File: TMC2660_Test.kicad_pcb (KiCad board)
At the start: 2 copper layers, 62 parts, among them P101 CONN_4, P102 CONN_4, P103 CONN_2, P104 CONN_13X2, P105 CONN_4, P106 CONN_4, P107 CONN_1, P108 CONN_1, P109 CONN_1, P110 CONN_1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

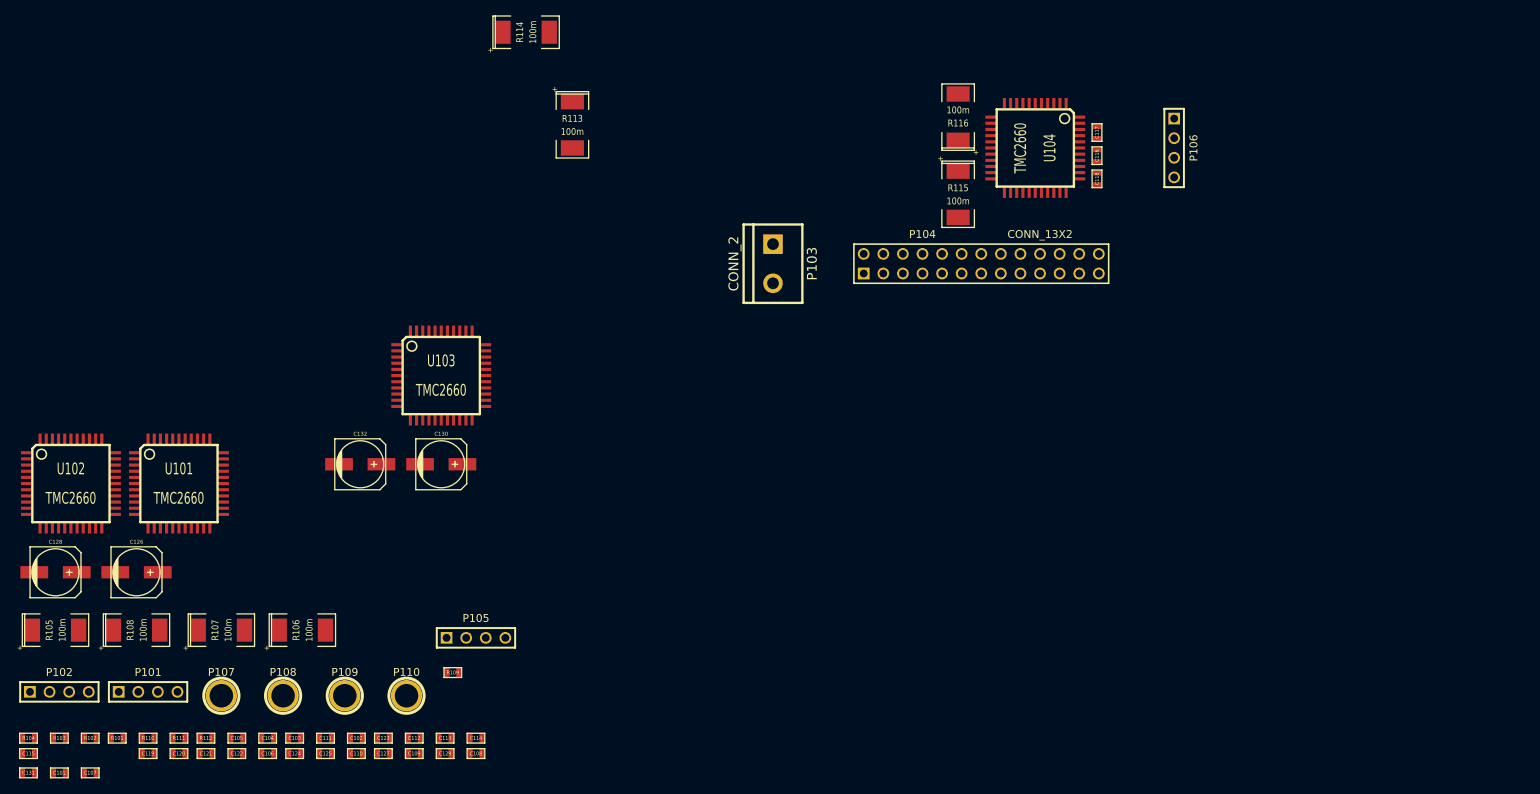
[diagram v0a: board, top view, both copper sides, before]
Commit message: Change alu. caps to thru hole.
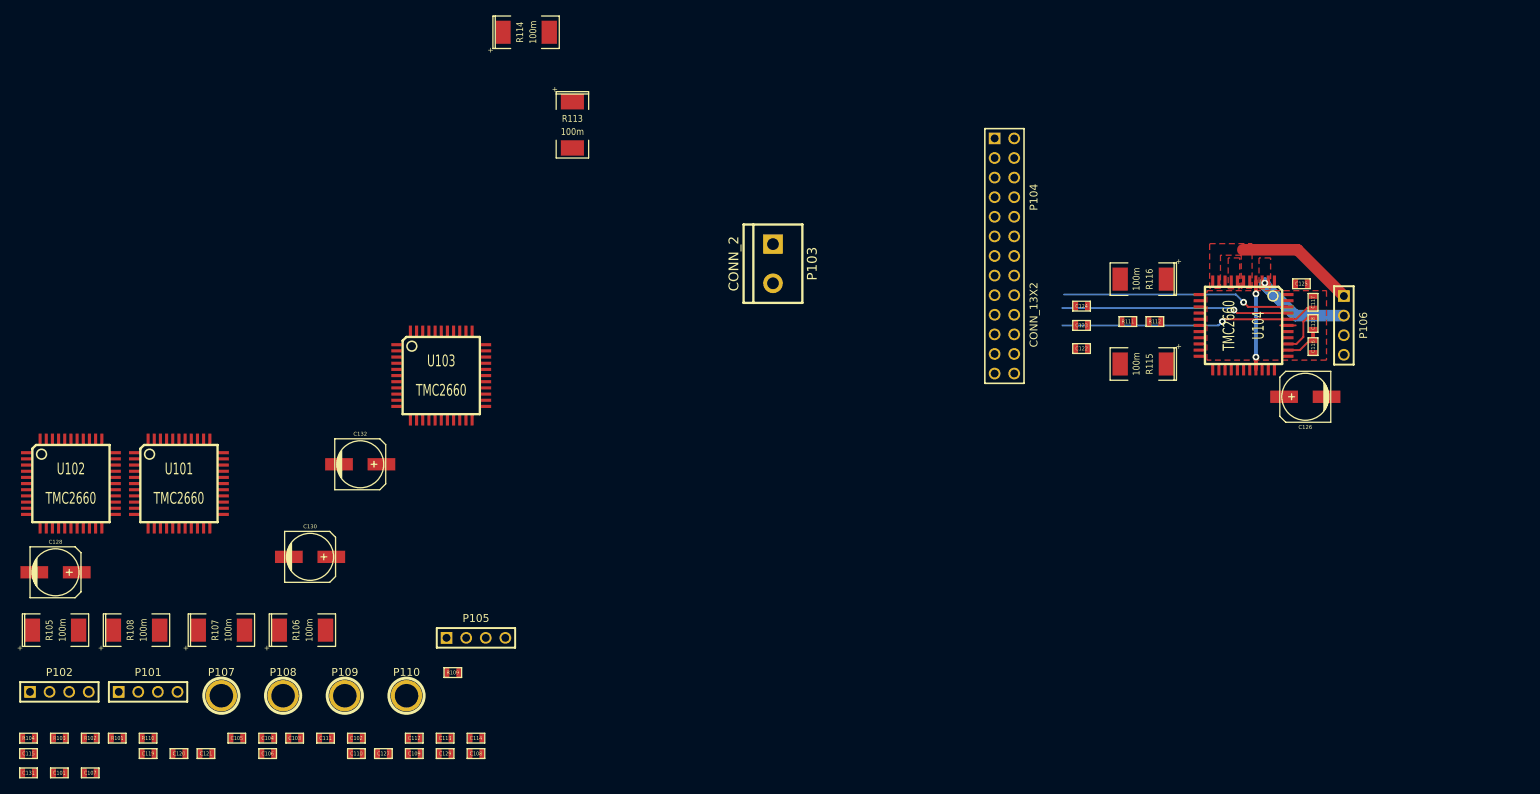
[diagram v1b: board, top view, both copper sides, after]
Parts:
- moved C126 153.2 mm to (185.0, 134.2), turned to 180 degrees
- moved C125 140.4 mm to (184.5, 119.6)
- moved R111 134.3 mm to (162.0, 124.5)
- moved R112 134.3 mm to (165.5, 124.5)
- moved C122 121.4 mm to (156.0, 128.0)
- moved C124 117.3 mm to (156.0, 122.5)
- moved C123 105.1 mm to (156.0, 125.0)
- moved C116 37.4 mm to (186.0, 127.8), turned to 90 degrees
- moved C117 35.6 mm to (186.0, 122.0)
- moved U104 35.5 mm to (177.0, 125.0)
- moved C118 33.7 mm to (186.0, 124.8), turned to 90 degrees
- moved R115 32.6 mm to (164.0, 130.0), turned to 180 degrees
- moved R116 31.9 mm to (164.0, 119.0), turned to 180 degrees
- moved P106 31.8 mm to (190.0, 125.0)
- moved C130 20.8 mm to (56.0, 155.0)
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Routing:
- net VCC: track 0.00 -> 33.4 mm, vias 0 -> 1
- net E-STEP: track 0.00 -> 29.6 mm, vias 0 -> 1
- net E-DIR: track 0.00 -> 29.5 mm, vias 0 -> 1
- net +12V: track 0.00 -> 16.7 mm, vias 0 -> 2
- net N-0000051: track 0.00 -> 15.6 mm
- net N-0000013: track 0.00 -> 12.1 mm, vias 0 -> 1
- net N-0000015: track 0.00 -> 5.87 mm
- net GND: track 0.00 -> 2.00 mm
- added copper zone on F.Cu, net GND
- added copper zone on F.Cu, net N-0000013
- added copper zone on F.Cu, net N-0000051
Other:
- net class Default: clearance 0.254 -> 0.152
- rule trace_clearance: 0.254 -> 0.152
- rule trace_min: 0.254 -> 0.154

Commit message: One chip sorta laid out.
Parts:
- C126, C128, C130, C132: footprint c_elec_6.3x7.7 -> C1V5
- moved C128 144.2 mm to (162.6, 120.9), turned to 270 degrees
- moved C127 128.9 mm to (184.3, 130.4)
- moved C126 23.1 mm to (162.6, 128.5), turned to 90 degrees
- moved C123 16.8 mm to (171.2, 117.9), turned to 180 degrees
- moved C122 15.8 mm to (171.3, 131.9), turned to 180 degrees
- moved R111 13.9 mm to (171.8, 134.4), turned to 90 degrees
- moved C124 12.4 mm to (168.4, 121.5), turned to 180 degrees
- moved R112 10.8 mm to (171.7, 115.7), turned to 90 degrees
- moved R115 4.59 mm to (164.9, 134.5)
- moved R116 3.49 mm to (164.8, 115.6)
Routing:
- net +12V: track 16.7 -> 52.4 mm
- net GND: track 2.00 -> 34.9 mm, vias 0 -> 17
- net N-0000051: track 15.6 -> 0.00 mm
- net N-0000013: track 12.1 -> 0.00 mm, vias 1 -> 0
- net N-0000048: track 0.00 -> 11.5 mm
- net N-0000045: track 0.00 -> 11.4 mm
- net N-0000046: track 0.00 -> 7.74 mm
- net N-0000047: track 0.00 -> 7.65 mm
- net E-STEP: track 29.6 -> 24.0 mm
- net E-DIR: track 29.5 -> 24.6 mm
- net VCC: track 33.4 -> 28.6 mm
- net N-0000012: track 0.00 -> 2.25 mm
- added copper zone on B.Cu, net GND
- added copper zone on B.Cu, net N-0000013
- added copper zone on B.Cu, net N-0000049
- added copper zone on F.Cu, net N-0000049
- added copper zone on F.Cu, net N-0000050

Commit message: Getting the layout close to complete
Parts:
- added C133: 1u, SM0603, F.Cu at (204.0, 99.5)
- added C134: 47u, C1V5, F.Cu at (105.7, 178.1)
- added C135: 1u, SM0603, F.Cu at (94.1, 161.7)
- added C136: 47u, C1V5, F.Cu at (87.0, 180.8)
- added C137: 1u, SM0603, F.Cu at (203.8, 111.7)
- added C138: 47u, C1V5, F.Cu at (109.7, 165.4)
- added C139: 1u, SM0603, F.Cu at (93.7, 163.5)
- added C140: 47u, C1V5, F.Cu at (92.5, 172.6)
- moved P102 198.0 mm to (209.8, 105.4), turned to 270 degrees
- moved R104 190.8 mm to (191.5, 95.9), turned to 90 degrees
- moved R103 179.5 mm to (191.4, 114.9), turned to 90 degrees
- moved U102 176.4 mm to (196.8, 105.4), turned to 270 degrees
- moved C104 172.8 mm to (205.7, 102.5), turned to 270 degrees
- moved C106 172.4 mm to (205.7, 105.4), turned to 90 degrees
- moved R108 166.0 mm to (184.8, 96.1), turned to 180 degrees
- moved C102 159.8 mm to (205.6, 108.5), turned to 90 degrees
- moved C110 152.9 mm to (191.0, 98.5), turned to 180 degrees
- moved R107 148.6 mm to (184.4, 114.3), turned to 180 degrees
- moved C112 140.4 mm to (187.8, 102.9)
- moved C109 139.5 mm to (190.9, 111.7), turned to 180 degrees
- moved C130 135.3 mm to (183.2, 108.9), turned to 90 degrees
- moved C132 127.7 mm to (183.2, 101.2), turned to 270 degrees
- moved P103 61.6 mm to (174.0, 137.8), turned to 0 degrees
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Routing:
- net GND: track 34.9 -> 22.5 mm, vias 17 -> 9
- added copper zone on F.Cu, net N-0000013
- added copper zone on F.Cu, net N-0000028
- added copper zone on B.Cu, net N-0000077
- added copper zone on F.Cu, net N-0000077
- added copper zone on B.Cu, net N-0000082
- added copper zone on F.Cu, net N-0000082
- added copper zone on F.Cu, net N-0000083
- added copper zone on F.Cu, net N-0000089
- removed copper zone on B.Cu, net GND
- removed copper zone on F.Cu, net N-0000018

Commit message: Everything is approximately where it should be. Now to draw all the damn fills and lines.
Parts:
- moved P107 168.8 mm to (209.8, 138.8), turned to 90 degrees
- moved P110 161.3 mm to (209.8, 95.3), turned to 90 degrees
- moved C107 155.7 mm to (157.2, 96.8), turned to 90 degrees
- moved R105 155.0 mm to (164.7, 101.8)
- moved R101 149.5 mm to (157.9, 99.5), turned to 180 degrees
- moved R102 146.8 mm to (158.0, 111.2)
- moved C101 143.9 mm to (142.6, 102.3), turned to 270 degrees
- moved C131 143.4 mm to (143.6, 111.2), turned to 180 degrees
- moved C119 135.6 mm to (156.7, 120.8), turned to 90 degrees
- moved C115 133.1 mm to (142.8, 130.3), turned to 270 degrees
- moved R110 130.0 mm to (158.0, 136.4)
- moved C121 126.4 mm to (159.8, 133.5)
- moved C120 125.5 mm to (157.4, 139.0), turned to 270 degrees
- moved C111 124.3 mm to (160.0, 107.5), turned to 90 degrees
- moved R106 123.7 mm to (165.6, 109.1)
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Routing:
- net VCC: track 28.6 -> 69.0 mm
- net +12V: track 52.4 -> 19.6 mm, vias 2 -> 0
- net GND: track 22.5 -> 9.05 mm, vias 9 -> 0
- net E-STEP: track 24.0 -> 30.3 mm
- net N-0000047: track 11.5 -> 5.96 mm
- net E-DIR: track 24.6 -> 29.7 mm
- net N-0000048: track 11.4 -> 7.52 mm
- net N-0000049: track 7.74 -> 6.37 mm
- net N-0000046: track 7.65 -> 6.71 mm
- net N-0000016: track 2.25 -> 2.84 mm
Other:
- board outline added: 77.7 x 49.9 mm

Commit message: Work on filled zones.
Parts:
- moved R108 2.24 mm to (182.9, 101.3)
- moved C120 1.00 mm to (157.5, 138.0)
- moved C137 1.00 mm to (204.6, 111.1)
- moved R107 0.99 mm to (184.2, 109.2)
- moved R110 0.89 mm to (158.4, 135.6)
- moved C135 0.71 mm to (143.5, 124.2)
- moved P105 0.70 mm to (138.6, 129.8)
- moved U103 0.70 mm to (151.6, 129.8)
- moved C114 0.60 mm to (142.8, 132.7)
- moved C115 0.60 mm to (142.8, 129.7)
- moved C113 0.60 mm to (142.8, 126.8)
- moved C112 0.32 mm to (188.4, 101.3)
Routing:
- net +12V: track 19.6 -> 285.4 mm
- net N-0000087: track 0.00 -> 7.05 mm
- net N-0000085: track 0.00 -> 6.90 mm
- net N-0000086: track 0.00 -> 6.84 mm
- net N-0000084: track 0.00 -> 5.61 mm
- net N-0000088: track 0.00 -> 5.52 mm
- net GND: track 9.05 -> 13.6 mm
- net VCC: track 69.0 -> 72.8 mm
- added copper zone on B.Cu, net N-0000063
- added copper zone on F.Cu, net N-0000063
- added copper zone on B.Cu, net N-0000073

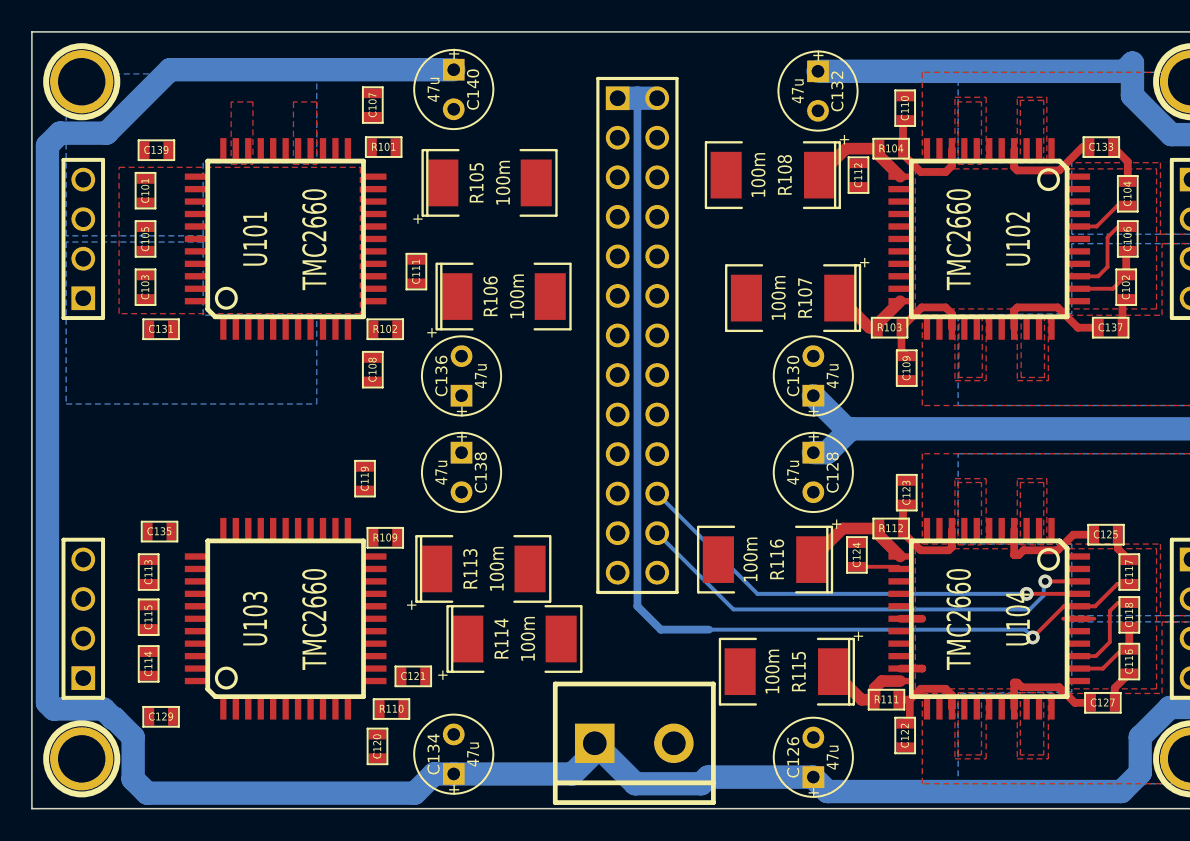
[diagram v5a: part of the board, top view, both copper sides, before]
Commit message: Finished all the power connections and varios R and Cs connected to the chips. Still to do: ground plane, signal lines, connect motor planes properly.
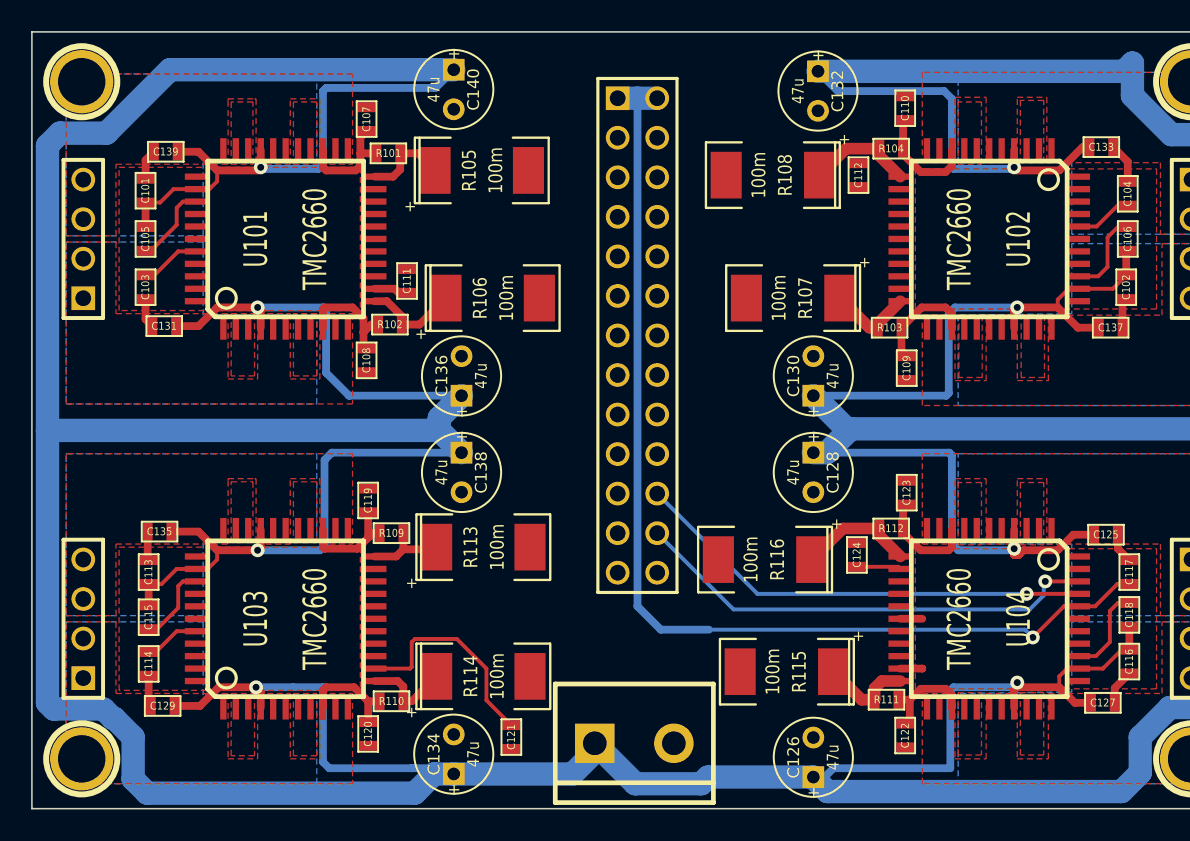
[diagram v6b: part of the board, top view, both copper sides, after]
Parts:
- moved C121 7.41 mm to (166.1, 137.4), turned to 270 degrees
- moved R114 3.12 mm to (164.3, 133.5)
- moved C119 1.41 mm to (156.9, 122.2)
- moved R113 1.40 mm to (164.3, 125.2)
- moved C120 1.00 mm to (156.9, 137.2)
- moved C107 0.98 mm to (156.8, 97.7)
- moved R105 0.94 mm to (164.2, 101.0)
- moved C111 0.85 mm to (159.4, 108.1)
- moved C108 0.72 mm to (156.8, 113.2)
- moved R106 0.71 mm to (164.9, 109.2)
- moved C129 0.71 mm to (143.7, 135.4)
- moved C139 0.61 mm to (143.9, 99.8)
- moved R109 0.50 mm to (158.4, 124.3)
- moved R110 0.50 mm to (158.4, 135.1)
- moved R101 0.50 mm to (158.2, 99.9)
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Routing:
- net +12V: track 285.4 -> 508.9 mm, vias 0 -> 8
- net N-0000020: track 0.00 -> 14.0 mm
- net VCC: track 72.8 -> 80.3 mm
- net N-0000052: track 0.00 -> 7.31 mm
- net N-0000054: track 0.00 -> 7.16 mm
- net N-0000022: track 0.00 -> 6.85 mm
- net N-0000023: track 0.00 -> 6.55 mm
- net N-0000056: track 0.00 -> 6.23 mm
- net GND: track 13.6 -> 19.4 mm
- net N-0000021: track 0.00 -> 5.74 mm
- net N-0000053: track 0.00 -> 5.57 mm
- net N-0000019: track 0.00 -> 5.27 mm
- net N-0000068: track 0.00 -> 5.24 mm
- net N-0000079: track 0.00 -> 5.17 mm
- net N-0000055: track 0.00 -> 2.19 mm
- added copper zone on B.Cu, net N-0000024
- added copper zone on F.Cu, net N-0000024
- added copper zone on B.Cu, net N-0000025
- added copper zone on F.Cu, net N-0000025
- added copper zone on F.Cu, net N-0000026
- added copper zone on F.Cu, net N-0000027
- added copper zone on F.Cu, net N-0000062
- added copper zone on F.Cu, net N-0000071
- added copper zone on F.Cu, net N-0000073

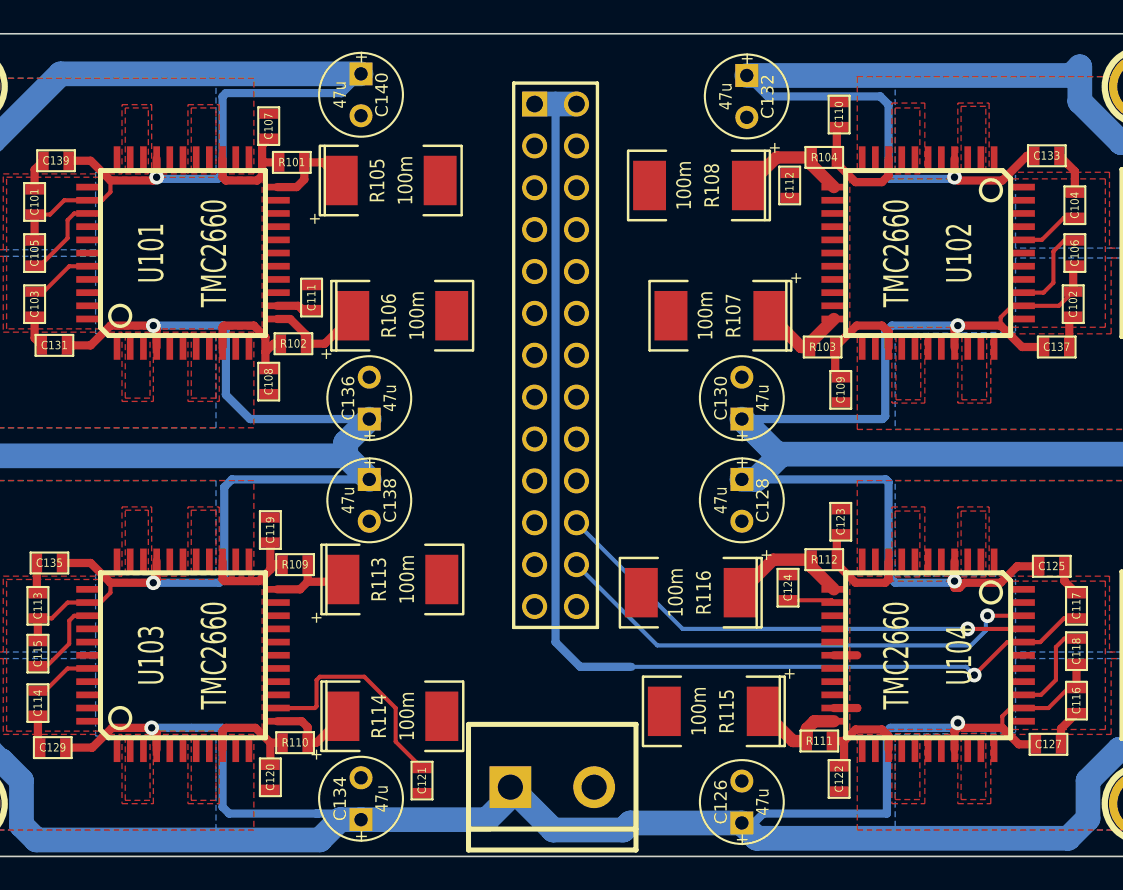
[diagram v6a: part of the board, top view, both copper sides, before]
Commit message: Add ground plane, begin adding signal traces.
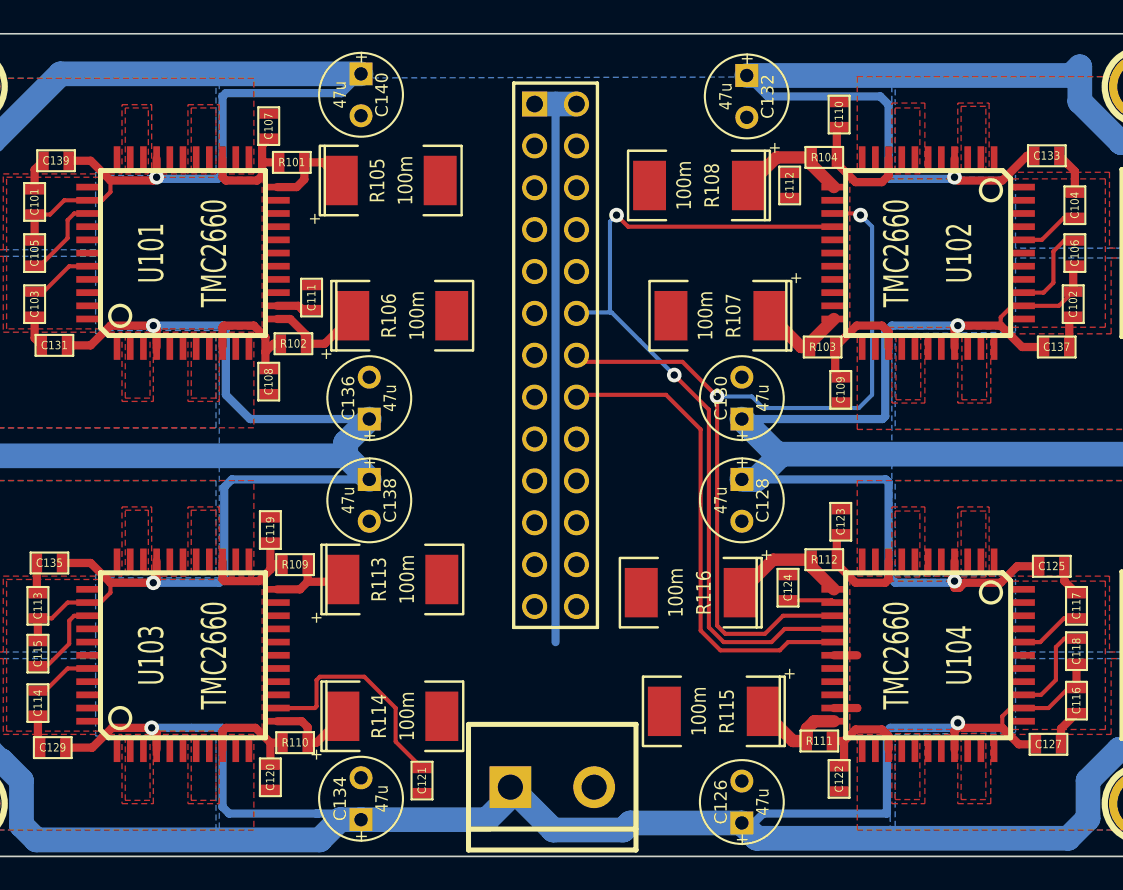
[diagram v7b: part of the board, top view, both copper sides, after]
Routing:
- net MISO: track 0.00 -> 54.1 mm, vias 0 -> 2
- net MOSI: track 0.00 -> 51.5 mm, vias 0 -> 2
- net E-STEP: track 30.3 -> 0.00 mm, vias 1 -> 0
- net VCC: track 80.3 -> 50.4 mm, vias 1 -> 0
- net E-DIR: track 29.7 -> 0.00 mm, vias 1 -> 0
- net SCK: track 0.00 -> 29.4 mm
- added copper zone on B.Cu, net GND
